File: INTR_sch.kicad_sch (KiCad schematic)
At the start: 14 parts, among them J10 Conn_01x04_Male, J11 Conn_01x03_Male, J12 Conn_01x03_Male, J13 Conn_01x02_Male, SW2 SW_Push, U13 PAL16L8, U14 16550, U18 8259A, U19 PAL16L8, U20 pkd8279, U21 8254

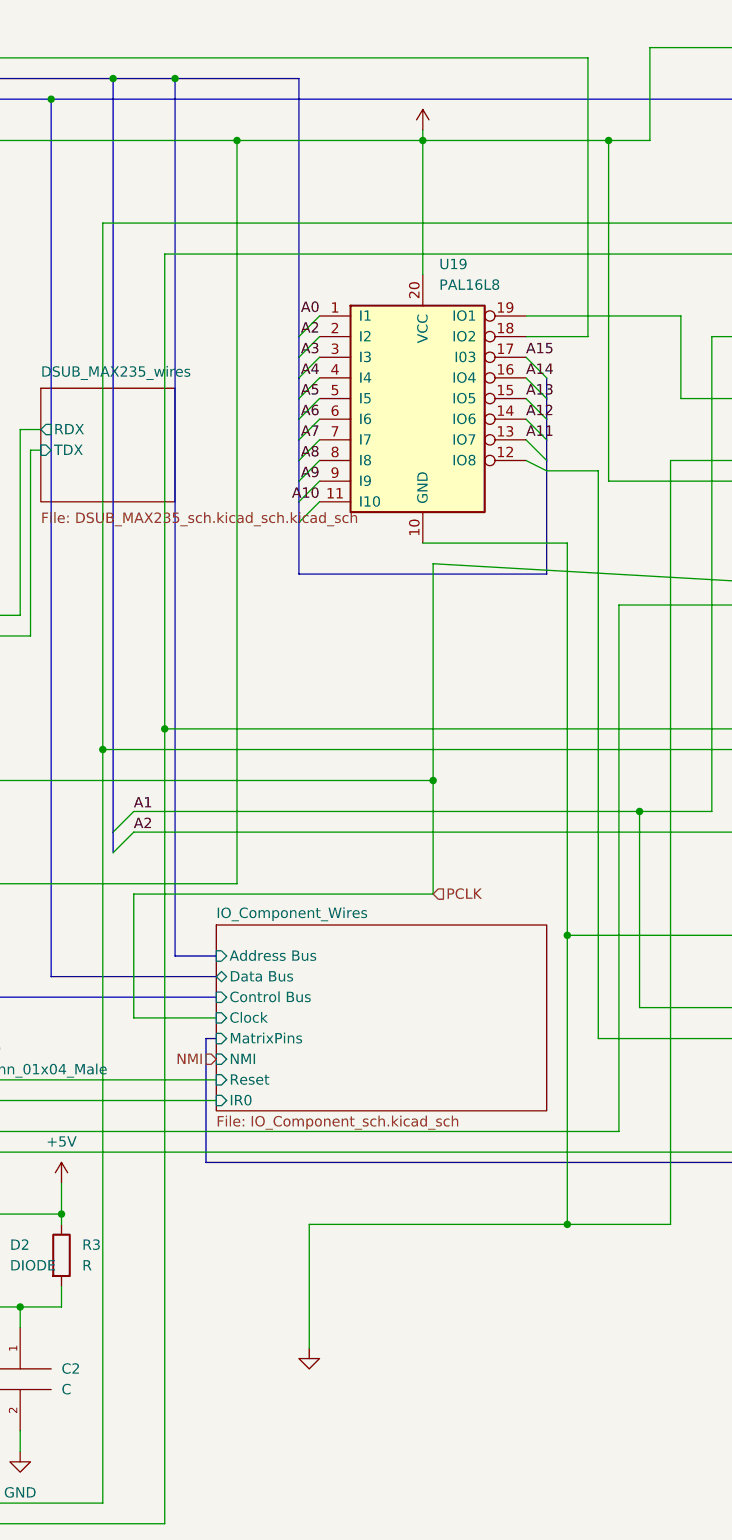
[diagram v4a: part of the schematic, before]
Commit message: Enabled inputs on the max235
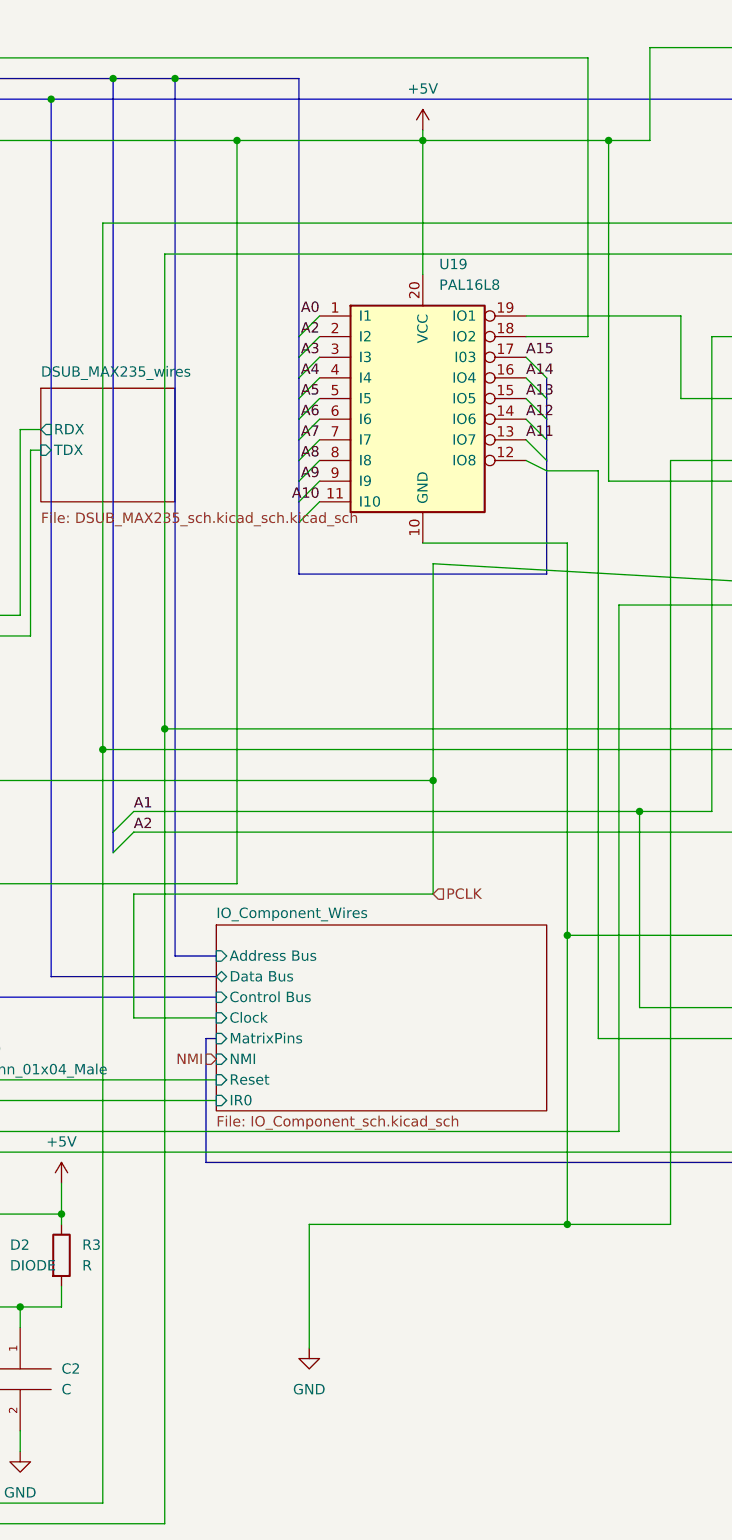
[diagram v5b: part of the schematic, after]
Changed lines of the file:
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@@
       (effects (font (size 1.27 1.27)) hide)
     )
-    (property "Value" "" (id 1) (at 166.37 179.07 0))
+    (property "Value" "GND" (id 1) (at 166.37 179.07 0))
     (property "Footprint" "" (id 2) (at 166.37 173.99 0)
       (effects (font (size 1.27 1.27)) hide)
@@
       (effects (font (size 1.27 1.27)) hide)
     )
-    (property "Value" "" (id 1) (at 180.34 19.05 0))
+    (property "Value" "+5V" (id 1) (at 180.34 19.05 0))
     (property "Footprint" "" (id 2) (at 180.34 24.13 0)
       (effects (font (size 1.27 1.27)) hide)

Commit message: Updated PCB
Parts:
- C2: value C -> (none); footprint Capacitor_SMD:CP_Elec_3x5.3 -> (none)
- D2: value DIODE -> (none); footprint Diode_SMD:D_0201_0603Metric -> (none)
- J10: value Conn_01x04_Male -> (none); footprint Connector_Harwin:Harwin_M20-89008xx_1x08_P2.54mm_Horizontal -> (none)
- J11, J12: value Conn_01x03_Male -> (none); footprint Connector_Harwin:Harwin_M20-89008xx_1x08_P2.54mm_Horizontal -> (none)
- J13: value Conn_01x02_Male -> (none); footprint Connector_Harwin:Harwin_M20-89008xx_1x08_P2.54mm_Horizontal -> (none)
- R3: value R -> (none); footprint Resistor_SMD:R_0201_0603Metric -> (none)
- SW2: value SW_Push -> (none); footprint Button_Switch_Keyboard:SW_Cherry_MX_1.00u_PCB -> (none)
- U13, U19: value PAL16L8 -> (none); footprint Package_DIP:DIP-20_W7.62mm -> (none)
- U14: value 16550 -> (none); footprint Package_DIP:DIP-40_W15.24mm -> (none)
- U18: value 8259A -> (none); footprint Package_DIP:DIP-28_W15.24mm -> (none)
- U20: value pkd8279 -> (none); footprint parts:pkd8279 -> (none)
- U21: value 8254 -> (none); footprint Package_DIP:DIP-24_W15.24mm -> (none)
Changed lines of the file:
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@@
       (effects (font (size 1.27 1.27)) (justify left))
     )
-    (property "Value" "16550" (id 1) (at 97.2694 26.67 0)
-      (effects (font (size 1.27 1.27)) (justify left))
-    )
-    (property "Footprint" "Package_DIP:DIP-40_W15.24mm" (id 2) (at 95.25 68.58 0)
+    (property "Value" "" (id 1) (at 97.2694 26.67 0)
+      (effects (font (size 1.27 1.27)) (justify left))
+    )
+    (property "Footprint" "" (id 2) (at 95.25 68.58 0)
       (effects (font (size 1.27 1.27) italic) hide)
     )
@@
       (effects (font (size 1.27 1.27)) (justify right))
     )
-    (property "Value" "Conn_01x02_Male" (id 1) (at 284.48 52.0699 0)
-      (effects (font (size 1.27 1.27)) (justify right))
-    )
-    (property "Footprint" "Connector_Harwin:Harwin_M20-89008xx_1x08_P2.54mm_Horizontal" (id 2) (at 283.21 52.07 0)
+    (property "Value" "" (id 1) (at 284.48 52.0699 0)
+      (effects (font (size 1.27 1.27)) (justify right))
+    )
+    (property "Footprint" "" (id 2) (at 283.21 52.07 0)
       (effects (font (size 1.27 1.27)) hide)
     )
@@
       (effects (font (size 1.27 1.27)) (justify right))
     )
-    (property "Value" "Conn_01x04_Male" (id 1) (at 125.73 139.6999 0)
-      (effects (font (size 1.27 1.27)) (justify right))
-    )
-    (property "Footprint" "Connector_Harwin:Harwin_M20-89008xx_1x08_P2.54mm_Horizontal" (id 2) (at 124.46 139.7 0)
+    (property "Value" "" (id 1) (at 125.73 139.6999 0)
+      (effects (font (size 1.27 1.27)) (justify right))
+    )
+    (property "Footprint" "" (id 2) (at 124.46 139.7 0)
       (effects (font (size 1.27 1.27)) hide)
     )
@@
       (effects (font (size 1.27 1.27)) (justify left))
     )
-    (property "Value" "PAL16L8" (id 1) (at 36.3094 92.71 0)
-      (effects (font (size 1.27 1.27)) (justify left))
-    )
-    (property "Footprint" "Package_DIP:DIP-20_W7.62mm" (id 2) (at 34.29 109.22 0)
+    (property "Value" "" (id 1) (at 36.3094 92.71 0)
+      (effects (font (size 1.27 1.27)) (justify left))
+    )
+    (property "Footprint" "" (id 2) (at 34.29 109.22 0)
       (effects (font (size 1.27 1.27)) hide)
     )
@@
       (effects (font (size 1.27 1.27)) (justify left))
     )
-    (property "Value" "R" (id 1) (at 138.43 163.8299 0)
-      (effects (font (size 1.27 1.27)) (justify left))
-    )
-    (property "Footprint" "Resistor_SMD:R_0201_0603Metric" (id 2) (at 134.112 162.56 90)
+    (property "Value" "" (id 1) (at 138.43 163.8299 0)
+      (effects (font (size 1.27 1.27)) (justify left))
+    )
+    (property "Footprint" "" (id 2) (at 134.112 162.56 90)
       (effects (font (size 1.27 1.27)) hide)
     )
@@
       (effects (font (size 1.27 1.27)) (justify left))
     )
-    (property "Value" "C" (id 1) (at 135.89 179.0699 0)
-      (effects (font (size 1.27 1.27)) (justify left))
-    )
-    (property "Footprint" "Capacitor_SMD:CP_Elec_3x5.3" (id 2) (at 130.81 177.8 0)
+    (property "Value" "" (id 1) (at 135.89 179.0699 0)
+      (effects (font (size 1.27 1.27)) (justify left))
+    )
+    (property "Footprint" "" (id 2) (at 130.81 177.8 0)
       (effects (font (size 1.27 1.27)) hide)
     )
@@
   (symbol (lib_id "power:GND") (at 166.37 173.99 0) (unit 1)
     (in_bom yes) (on_board yes) (fields_autoplaced)
-    (property "Reference" "#PWR?" (id 0) (at 166.37 180.34 0)
+    (property "Reference" "#PWR0126" (id 0) (at 166.37 180.34 0)
       (effects (font (size 1.27 1.27)) hide)
     )
@@
       (effects (font (size 1.27 1.27)) (justify left))
     )
-    (property "Value" "8259A" (id 1) (at 93.4594 128.27 0)
-      (effects (font (size 1.27 1.27)) (justify left))
-    )
-    (property "Footprint" "Package_DIP:DIP-28_W15.24mm" (id 2) (at 91.44 154.94 0)
+    (property "Value" "" (id 1) (at 93.4594 128.27 0)
+      (effects (font (size 1.27 1.27)) (justify left))
+    )
+    (property "Footprint" "" (id 2) (at 91.44 154.94 0)
       (effects (font (size 1.27 1.27) italic) hide)
     )
@@
       (effects (font (size 1.27 1.27)) (justify right))
     )
-    (property "Value" "DIODE" (id 1) (at 129.54 163.8299 90)
-      (effects (font (size 1.27 1.27)) (justify right))
-    )
-    (property "Footprint" "Diode_SMD:D_0201_0603Metric" (id 2) (at 125.73 162.56 0)
+    (property "Value" "" (id 1) (at 129.54 163.8299 90)
+      (effects (font (size 1.27 1.27)) (justify right))
+    )
+    (property "Footprint" "" (id 2) (at 125.73 162.56 0)
       (effects (font (size 1.27 1.27)) hide)
     )
@@
       (effects (font (size 1.27 1.27)) (justify left))
     )
-    (property "Value" "PAL16L8" (id 1) (at 182.3594 43.18 0)
-      (effects (font (size 1.27 1.27)) (justify left))
-    )
-    (property "Footprint" "Package_DIP:DIP-20_W7.62mm" (id 2) (at 180.34 59.69 0)
+    (property "Value" "" (id 1) (at 182.3594 43.18 0)
+      (effects (font (size 1.27 1.27)) (justify left))
+    )
+    (property "Footprint" "" (id 2) (at 180.34 59.69 0)
       (effects (font (size 1.27 1.27)) hide)
     )
@@
       (effects (font (size 1.27 1.27)) (justify left))
     )
-    (property "Value" "8254" (id 1) (at 266.1794 13.97 0)
-      (effects (font (size 1.27 1.27)) (justify left))
-    )
-    (property "Footprint" "Package_DIP:DIP-24_W15.24mm" (id 2) (at 264.16 39.37 0)
+    (property "Value" "" (id 1) (at 266.1794 13.97 0)
+      (effects (font (size 1.27 1.27)) (justify left))
+    )
+    (property "Footprint" "" (id 2) (at 264.16 39.37 0)
       (effects (font (size 1.27 1.27)) hide)
     )
@@
   (symbol (lib_id "power:+5V") (at 180.34 24.13 0) (unit 1)
     (in_bom yes) (on_board yes) (fields_autoplaced)
-    (property "Reference" "#PWR?" (id 0) (at 180.34 27.94 0)
+    (property "Reference" "#PWR0127" (id 0) (at 180.34 27.94 0)
       (effects (font (size 1.27 1.27)) hide)
     )
@@
     (in_bom yes) (on_board yes) (fields_autoplaced)
     (property "Reference" "SW2" (id 0) (at 118.11 161.29 0))
-    (property "Value" "SW_Push" (id 1) (at 118.11 163.83 0))
-    (property "Footprint" "Button_Switch_Keyboard:SW_Cherry_MX_1.00u_PCB" (id 2) (at 118.11 163.83 0)
+    (property "Value" "" (id 1) (at 118.11 163.83 0))
+    (property "Footprint" "" (id 2) (at 118.11 163.83 0)
       (effects (font (size 1.27 1.27)) hide)
     )
@@
       (effects (font (size 1.27 1.27)) (justify right))
     )
-    (property "Value" "Conn_01x03_Male" (id 1) (at 284.48 40.6399 0)
-      (effects (font (size 1.27 1.27)) (justify right))
-    )
-    (property "Footprint" "Connector_Harwin:Harwin_M20-89008xx_1x08_P2.54mm_Horizontal" (id 2) (at 283.21 39.37 0)
+    (property "Value" "" (id 1) (at 284.48 40.6399 0)
+      (effects (font (size 1.27 1.27)) (justify right))
+    )
+    (property "Footprint" "" (id 2) (at 283.21 39.37 0)
       (effects (font (size 1.27 1.27)) hide)
     )
@@
       (effects (font (size 1.524 1.524)))
     )
-    (property "Value" "pkd8279" (id 1) (at 252.095 67.31 0)
+    (property "Value" "" (id 1) (at 252.095 67.31 0)
       (effects (font (size 1.524 1.524)))
     )
-    (property "Footprint" "parts:pkd8279" (id 2) (at 251.46 65.024 0)
+    (property "Footprint" "" (id 2) (at 251.46 65.024 0)
       (effects (font (size 1.524 1.524)) hide)
     )
@@
       (effects (font (size 1.27 1.27)) (justify right))
     )
-    (property "Value" "Conn_01x03_Male" (id 1) (at 284.48 27.9399 0)
-      (effects (font (size 1.27 1.27)) (justify right))
-    )
-    (property "Footprint" "Connector_Harwin:Harwin_M20-89008xx_1x08_P2.54mm_Horizontal" (id 2) (at 283.21 26.67 0)
-      (effects (font (size 1.27 1.27)) hide)
-    )
+    (property "Value" "" (id 1) (at 284.48 27.9399 0)
+      (effects (font (size 1.27 1.27)) (justify right))
+    )
+    (property "Footprint" "" (id 2) (at 283.21 26.67 0)
+      (effects (font (size 1.27 1.27)) hide)
+    )

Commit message: PCB wiring
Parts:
- C2: value (none) -> C; footprint (none) -> Capacitor_SMD:CP_Elec_3x5.3
- D2: value (none) -> DIODE; footprint (none) -> Diode_SMD:D_0201_0603Metric
- J10: value (none) -> Conn_01x04_Male; footprint (none) -> Connector_Harwin:Harwin_M20-89008xx_1x08_P2.54mm_Horizontal
- J11, J12: value (none) -> Conn_01x03_Male; footprint (none) -> Connector_Harwin:Harwin_M20-89008xx_1x08_P2.54mm_Horizontal
- J13: value (none) -> Conn_01x02_Male; footprint (none) -> Connector_Harwin:Harwin_M20-89008xx_1x08_P2.54mm_Horizontal
- R3: value (none) -> R; footprint (none) -> Resistor_SMD:R_0201_0603Metric
- SW2: value (none) -> SW_Push; footprint (none) -> Button_Switch_Keyboard:SW_Cherry_MX_1.00u_PCB
- U13, U19: value (none) -> PAL16L8; footprint (none) -> Package_DIP:DIP-20_W7.62mm
- U14: value (none) -> 16550; footprint (none) -> Package_DIP:DIP-40_W15.24mm
- U18: value (none) -> 8259A; footprint (none) -> Package_DIP:DIP-28_W15.24mm
- U20: value (none) -> pkd8279; footprint (none) -> parts:pkd8279
- U21: value (none) -> 8254; footprint (none) -> Package_DIP:DIP-24_W15.24mm
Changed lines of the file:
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@@
       (effects (font (size 1.27 1.27)) (justify left))
     )
-    (property "Value" "" (id 1) (at 97.2694 26.67 0)
-      (effects (font (size 1.27 1.27)) (justify left))
-    )
-    (property "Footprint" "" (id 2) (at 95.25 68.58 0)
+    (property "Value" "16550" (id 1) (at 97.2694 26.67 0)
+      (effects (font (size 1.27 1.27)) (justify left))
+    )
+    (property "Footprint" "Package_DIP:DIP-40_W15.24mm" (id 2) (at 95.25 68.58 0)
       (effects (font (size 1.27 1.27) italic) hide)
     )
@@
       (effects (font (size 1.27 1.27)) (justify right))
     )
-    (property "Value" "" (id 1) (at 284.48 52.0699 0)
-      (effects (font (size 1.27 1.27)) (justify right))
-    )
-    (property "Footprint" "" (id 2) (at 283.21 52.07 0)
+    (property "Value" "Conn_01x02_Male" (id 1) (at 284.48 52.0699 0)
+      (effects (font (size 1.27 1.27)) (justify right))
+    )
+    (property "Footprint" "Connector_Harwin:Harwin_M20-89008xx_1x08_P2.54mm_Horizontal" (id 2) (at 283.21 52.07 0)
       (effects (font (size 1.27 1.27)) hide)
     )
@@
       (effects (font (size 1.27 1.27)) (justify right))
     )
-    (property "Value" "" (id 1) (at 125.73 139.6999 0)
-      (effects (font (size 1.27 1.27)) (justify right))
-    )
-    (property "Footprint" "" (id 2) (at 124.46 139.7 0)
+    (property "Value" "Conn_01x04_Male" (id 1) (at 125.73 139.6999 0)
+      (effects (font (size 1.27 1.27)) (justify right))
+    )
+    (property "Footprint" "Connector_Harwin:Harwin_M20-89008xx_1x08_P2.54mm_Horizontal" (id 2) (at 124.46 139.7 0)
       (effects (font (size 1.27 1.27)) hide)
     )
@@
       (effects (font (size 1.27 1.27)) (justify left))
     )
-    (property "Value" "" (id 1) (at 36.3094 92.71 0)
-      (effects (font (size 1.27 1.27)) (justify left))
-    )
-    (property "Footprint" "" (id 2) (at 34.29 109.22 0)
+    (property "Value" "PAL16L8" (id 1) (at 36.3094 92.71 0)
+      (effects (font (size 1.27 1.27)) (justify left))
+    )
+    (property "Footprint" "Package_DIP:DIP-20_W7.62mm" (id 2) (at 34.29 109.22 0)
       (effects (font (size 1.27 1.27)) hide)
     )
@@
       (effects (font (size 1.27 1.27)) (justify left))
     )
-    (property "Value" "" (id 1) (at 138.43 163.8299 0)
-      (effects (font (size 1.27 1.27)) (justify left))
-    )
-    (property "Footprint" "" (id 2) (at 134.112 162.56 90)
+    (property "Value" "R" (id 1) (at 138.43 163.8299 0)
+      (effects (font (size 1.27 1.27)) (justify left))
+    )
+    (property "Footprint" "Resistor_SMD:R_0201_0603Metric" (id 2) (at 134.112 162.56 90)
       (effects (font (size 1.27 1.27)) hide)
     )
@@
       (effects (font (size 1.27 1.27)) (justify left))
     )
-    (property "Value" "" (id 1) (at 135.89 179.0699 0)
-      (effects (font (size 1.27 1.27)) (justify left))
-    )
-    (property "Footprint" "" (id 2) (at 130.81 177.8 0)
+    (property "Value" "C" (id 1) (at 135.89 179.0699 0)
+      (effects (font (size 1.27 1.27)) (justify left))
+    )
+    (property "Footprint" "Capacitor_SMD:CP_Elec_3x5.3" (id 2) (at 130.81 177.8 0)
       (effects (font (size 1.27 1.27)) hide)
     )
@@
       (effects (font (size 1.27 1.27)) (justify left))
     )
-    (property "Value" "" (id 1) (at 93.4594 128.27 0)
-      (effects (font (size 1.27 1.27)) (justify left))
-    )
-    (property "Footprint" "" (id 2) (at 91.44 154.94 0)
+    (property "Value" "8259A" (id 1) (at 93.4594 128.27 0)
+      (effects (font (size 1.27 1.27)) (justify left))
+    )
+    (property "Footprint" "Package_DIP:DIP-28_W15.24mm" (id 2) (at 91.44 154.94 0)
       (effects (font (size 1.27 1.27) italic) hide)
     )
@@
       (effects (font (size 1.27 1.27)) (justify right))
     )
-    (property "Value" "" (id 1) (at 129.54 163.8299 90)
-      (effects (font (size 1.27 1.27)) (justify right))
-    )
-    (property "Footprint" "" (id 2) (at 125.73 162.56 0)
+    (property "Value" "DIODE" (id 1) (at 129.54 163.8299 90)
+      (effects (font (size 1.27 1.27)) (justify right))
+    )
+    (property "Footprint" "Diode_SMD:D_0201_0603Metric" (id 2) (at 125.73 162.56 0)
       (effects (font (size 1.27 1.27)) hide)
     )
@@
       (effects (font (size 1.27 1.27)) (justify left))
     )
-    (property "Value" "" (id 1) (at 182.3594 43.18 0)
-      (effects (font (size 1.27 1.27)) (justify left))
-    )
-    (property "Footprint" "" (id 2) (at 180.34 59.69 0)
+    (property "Value" "PAL16L8" (id 1) (at 182.3594 43.18 0)
+      (effects (font (size 1.27 1.27)) (justify left))
+    )
+    (property "Footprint" "Package_DIP:DIP-20_W7.62mm" (id 2) (at 180.34 59.69 0)
       (effects (font (size 1.27 1.27)) hide)
     )
@@
       (effects (font (size 1.27 1.27)) (justify left))
     )
-    (property "Value" "" (id 1) (at 266.1794 13.97 0)
-      (effects (font (size 1.27 1.27)) (justify left))
-    )
-    (property "Footprint" "" (id 2) (at 264.16 39.37 0)
+    (property "Value" "8254" (id 1) (at 266.1794 13.97 0)
+      (effects (font (size 1.27 1.27)) (justify left))
+    )
+    (property "Footprint" "Package_DIP:DIP-24_W15.24mm" (id 2) (at 264.16 39.37 0)
       (effects (font (size 1.27 1.27)) hide)
     )
@@
     (in_bom yes) (on_board yes) (fields_autoplaced)
     (property "Reference" "SW2" (id 0) (at 118.11 161.29 0))
-    (property "Value" "" (id 1) (at 118.11 163.83 0))
-    (property "Footprint" "" (id 2) (at 118.11 163.83 0)
+    (property "Value" "SW_Push" (id 1) (at 118.11 163.83 0))
+    (property "Footprint" "Button_Switch_Keyboard:SW_Cherry_MX_1.00u_PCB" (id 2) (at 118.11 163.83 0)
       (effects (font (size 1.27 1.27)) hide)
     )
@@
       (effects (font (size 1.27 1.27)) (justify right))
     )
-    (property "Value" "" (id 1) (at 284.48 40.6399 0)
-      (effects (font (size 1.27 1.27)) (justify right))
-    )
-    (property "Footprint" "" (id 2) (at 283.21 39.37 0)
+    (property "Value" "Conn_01x03_Male" (id 1) (at 284.48 40.6399 0)
+      (effects (font (size 1.27 1.27)) (justify right))
+    )
+    (property "Footprint" "Connector_Harwin:Harwin_M20-89008xx_1x08_P2.54mm_Horizontal" (id 2) (at 283.21 39.37 0)
       (effects (font (size 1.27 1.27)) hide)
     )
@@
       (effects (font (size 1.524 1.524)))
     )
-    (property "Value" "" (id 1) (at 252.095 67.31 0)
+    (property "Value" "pkd8279" (id 1) (at 252.095 67.31 0)
       (effects (font (size 1.524 1.524)))
     )
-    (property "Footprint" "" (id 2) (at 251.46 65.024 0)
+    (property "Footprint" "parts:pkd8279" (id 2) (at 251.46 65.024 0)
       (effects (font (size 1.524 1.524)) hide)
     )
@@
       (effects (font (size 1.27 1.27)) (justify right))
     )
-    (property "Value" "" (id 1) (at 284.48 27.9399 0)
-      (effects (font (size 1.27 1.27)) (justify right))
-    )
-    (property "Footprint" "" (id 2) (at 283.21 26.67 0)
-      (effects (font (size 1.27 1.27)) hide)
-    )
+    (property "Value" "Conn_01x03_Male" (id 1) (at 284.48 27.9399 0)
+      (effects (font (size 1.27 1.27)) (justify right))
+    )
+    (property "Footprint" "Connector_Harwin:Harwin_M20-89008xx_1x08_P2.54mm_Horizontal" (id 2) (at 283.21 26.67 0)
+      (effects (font (size 1.27 1.27)) hide)
+    )
